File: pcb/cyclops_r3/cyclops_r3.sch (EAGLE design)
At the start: 120 parts, among them Q1 BC817-16SMD, Q2 IRF540, U1 MCP4921, U10 AD829, U11 MIC5225, U12 MIC5270, U2 317-N, U3 TLV3701, U4 337-N, U5 ADR03, U6 OP1177, U7 TLV2374, U8 ZXTD45, U9 ADA4899

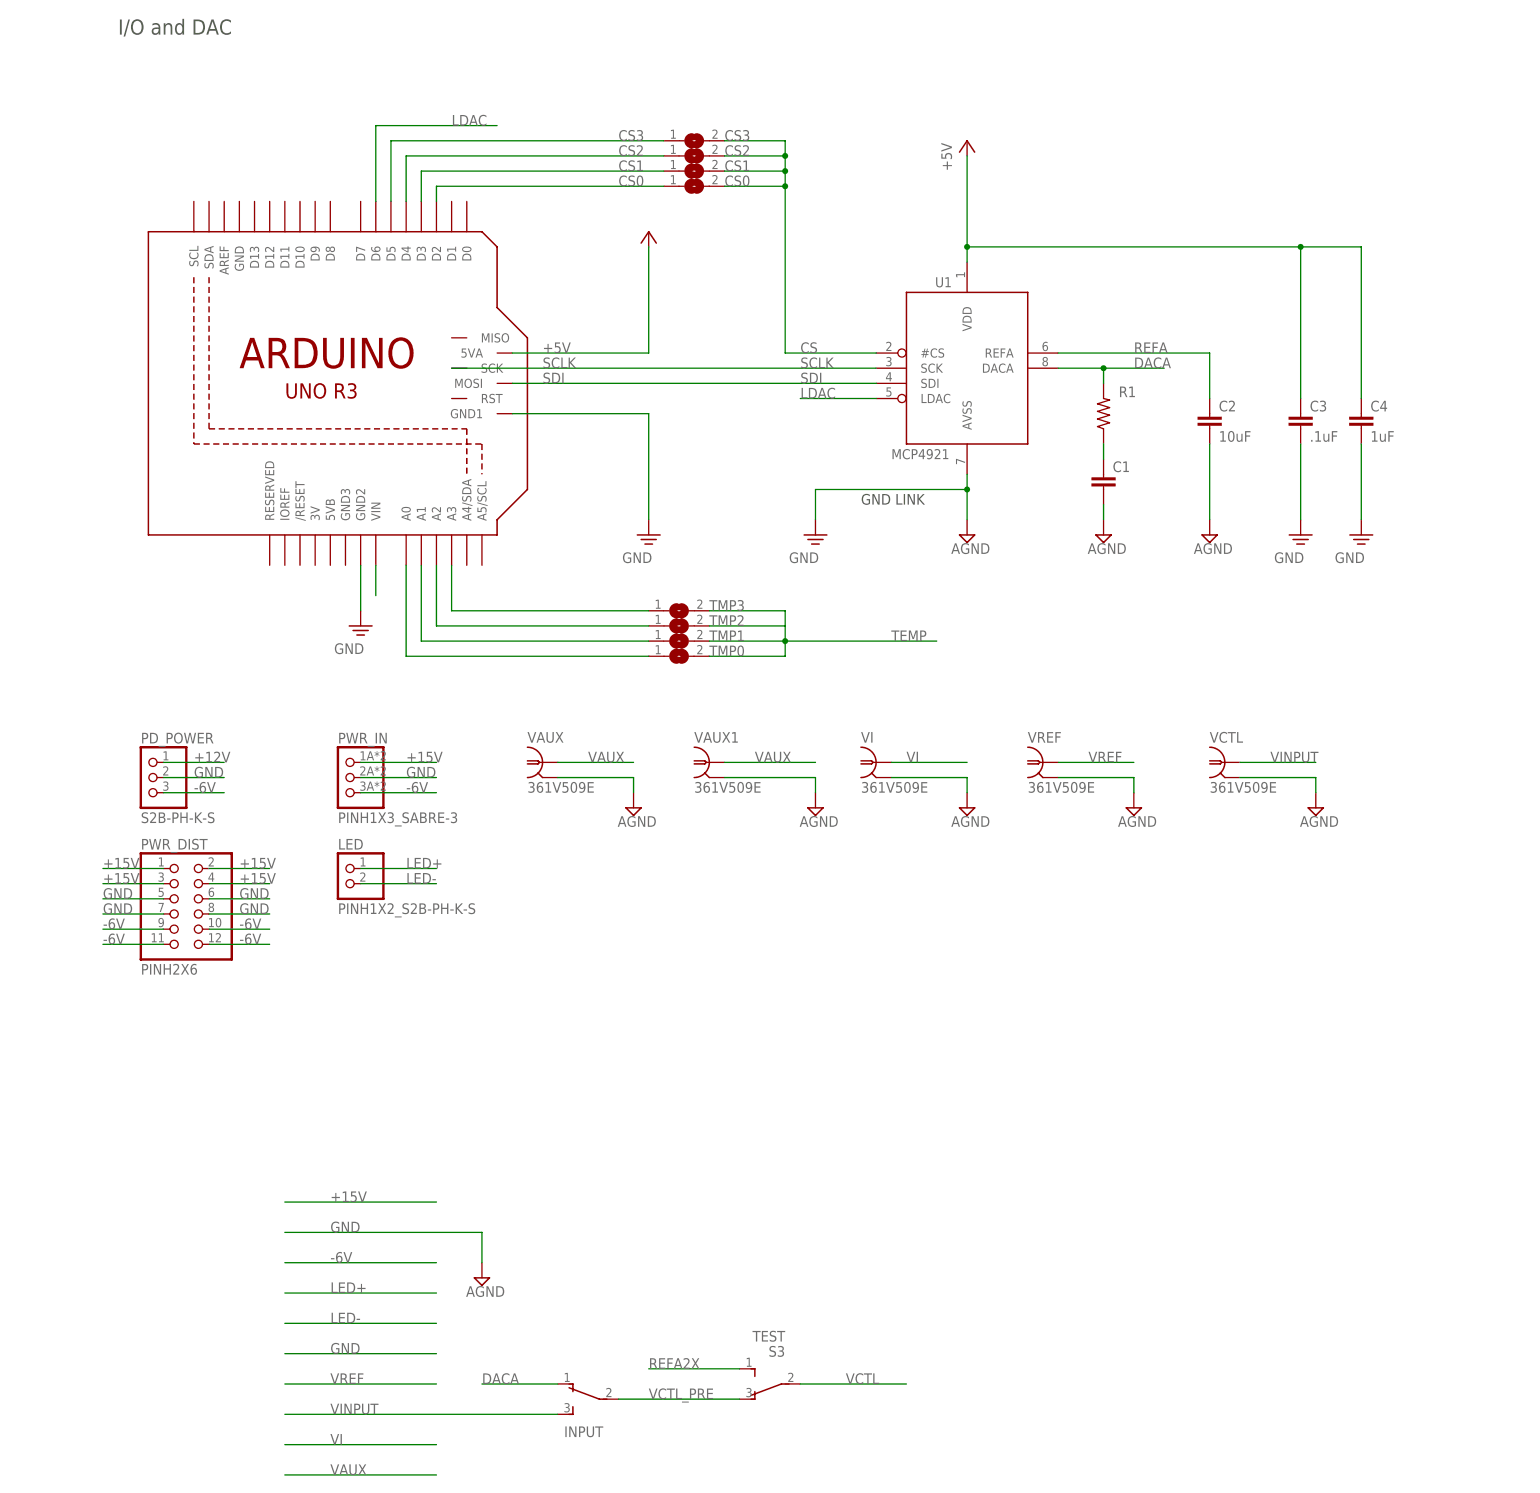
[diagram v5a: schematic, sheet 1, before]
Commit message: Finished basic layout. Need to go through notes and check things off. Need to perform ERC and DRC. Need to finish silkscreen.
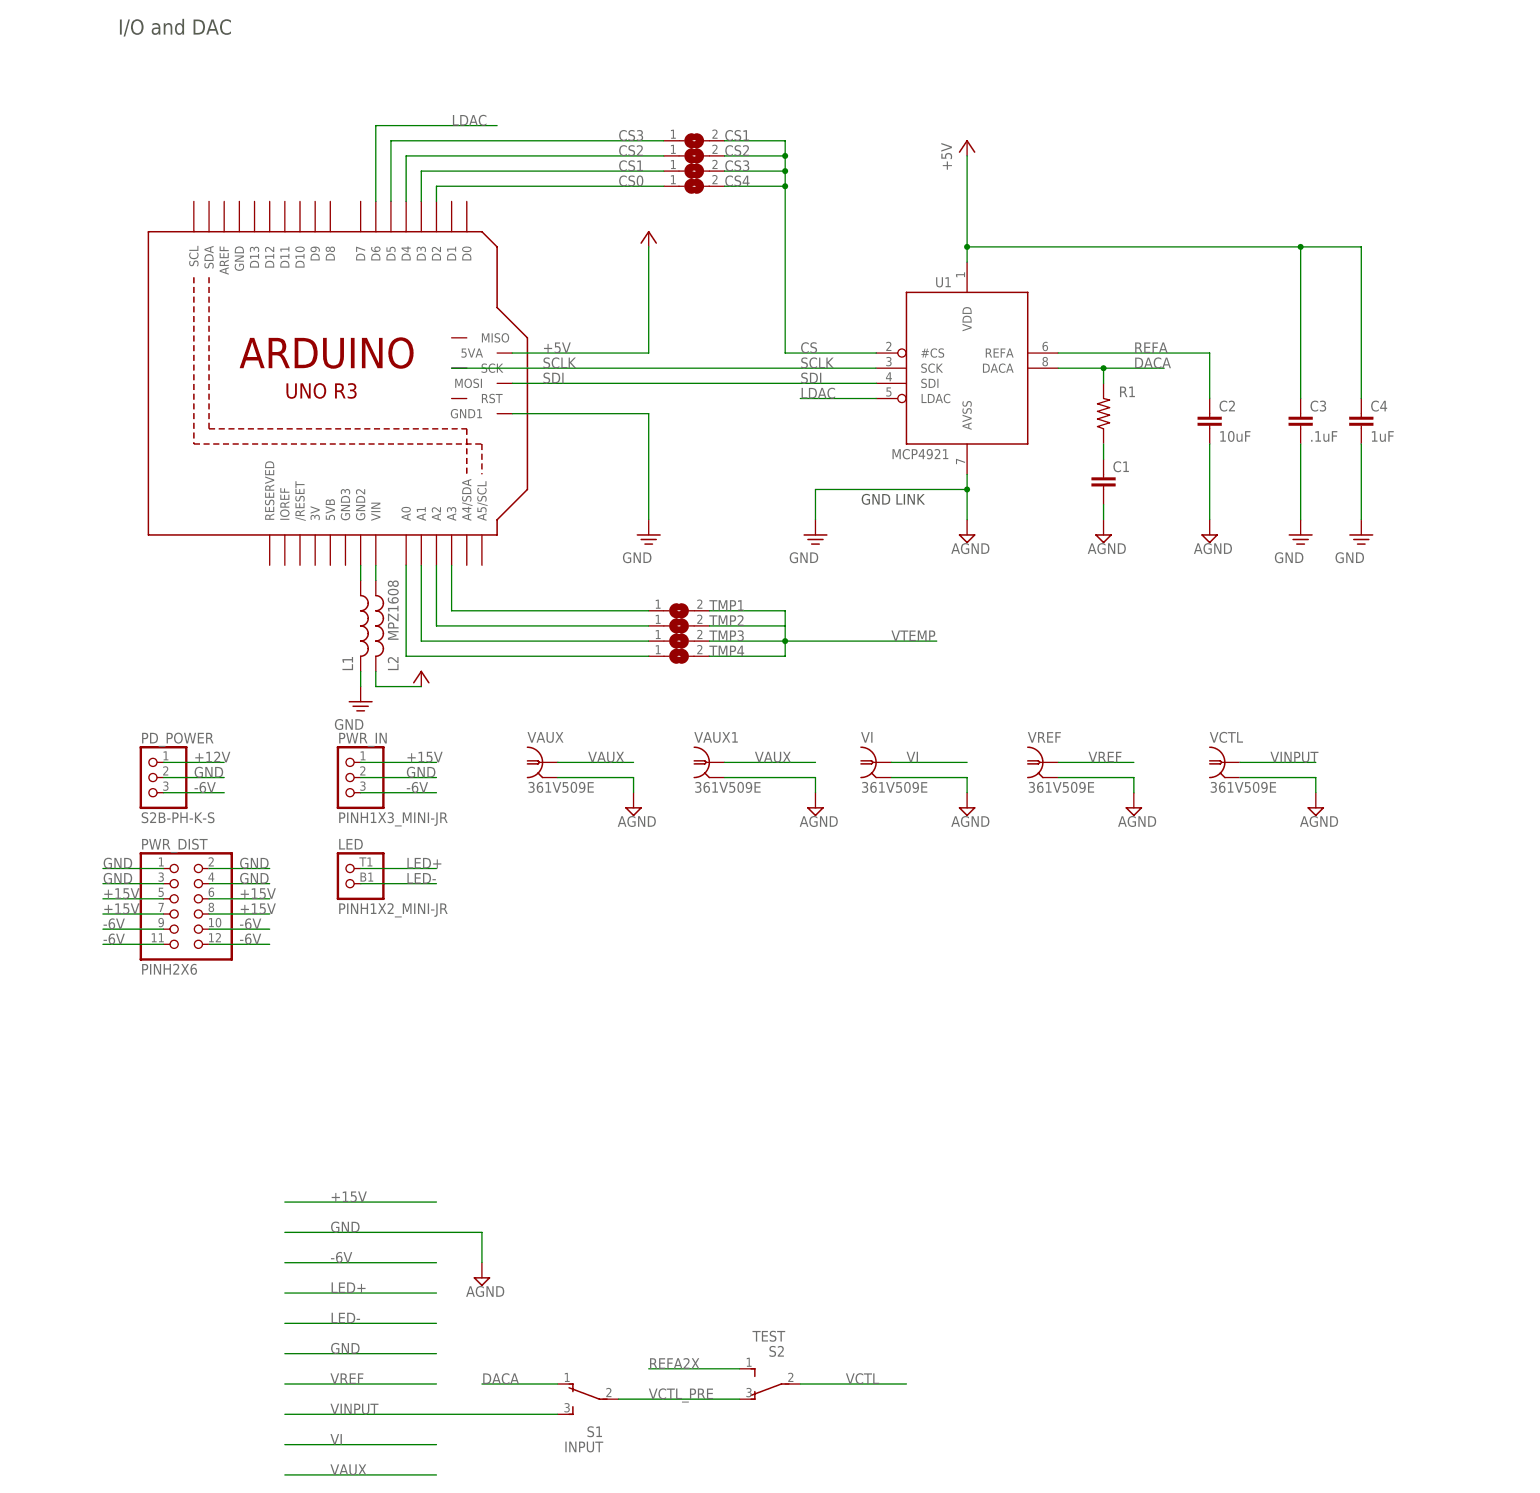
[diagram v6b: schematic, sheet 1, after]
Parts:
- removed D5: VBPW34S, cyclops:PHOTODIODE_VBPW34S
- removed R28: 140, cyclops:R_0603
- removed R29: 237, cyclops:R_0603
- removed R30: 79, cyclops:R_0603
- removed S5: CURR/AUX, cyclops:SPDT_JS
- added D1: S1B, cyclops:DIODES1B-13-F
- added L1, L2: MPZ1608, cyclops:L_0805
- added R10: 75, cyclops:R_0603
- added R6: 2.1k, cyclops:R_0603
- added R7: 10k, cyclops:R_0603
- added S2: TEST, cyclops:SPDT_CFPA
- C19: value .1uF -> (none)
- C20, C29, C34: value 1uF -> .1uF; device cyclops:C_0805 -> cyclops:C_0603
- C21: value (none) -> .1uF
- C23, C25: value 10uF -> 1uF; device cyclops:C-POL_6032M -> cyclops:C_0805
- C24: value 1uF -> 10uF; device cyclops:C_0805 -> cyclops:C-POL_6032M
- C26: value 15pF -> 10uF; device cyclops:C_0603 -> cyclops:C-POL_6032M
- C27: value .1uF -> 15pF
- C30: value 56pF -> 1uF; device cyclops:C_0603 -> cyclops:C_0805
- C31: value 1uF -> 56pF; device cyclops:C_0805 -> cyclops:C_0603
- C32: value .1uF -> 10pF
- C33, C36: value .1uF -> 1uF; device cyclops:C_0603 -> cyclops:C_0805
- C35: value 10pF -> .1uF
- D2: value S1B -> DS11015; device cyclops:DIODES1B-13-F -> cyclops:S-DIODESOD-123
- D4: value DS11015 -> VBPW34S; device cyclops:S-DIODESOD-123 -> cyclops:PHOTODIODE_VBPW34S
- LED: value PINH1X2_S2B-PH-K-S -> PINH1X2_MINI-JR; device cyclops:PINH1X2_S2B-PH-K-S -> cyclops:PINH1X2_MINI-JR
- PWR_IN: value PINH1X3_SABRE-3 -> PINH1X3_MINI-JR; device cyclops:PINH1X3_SABRE-3 -> cyclops:PINH1X3_MINI-JR
- R11: value 1k -> 120
- R12: value 3k -> 470
- R13: value 75 -> 1k
- R14: value 120 -> 1k
- R15: value 470 -> 1k
- R18: value 1k -> 9k 0.1%
- R19: value 1k -> 1k 0.1%
- R20: value 1k -> 10
- R21: value 1k 0.1% -> 1k
- R22: value 9k 0.1% -> 1.24k
- R23: value 10 -> 20k
- R24: value 1k -> 4.3k
- R25: value 1.24k -> 140
- R26: value 20k -> 237
- R27: value 4.3k -> 79
- R3: value 10k -> 110k
- R4: value 110k -> 10k
- R5: value 10k -> 240
- R8: value 240 -> 1k
- R9: value 2.1k -> 3k
- S1: value (none) -> INPUT
- S3: value TEST -> CURR/AUX; device cyclops:SPDT_CFPA -> cyclops:SPDT_JS
- U10: value AD829 -> MIC5225; device cyclops:AD829JRZ -> cyclops:MIC5225
- U11: value MIC5225 -> AD829; device cyclops:MIC5225 -> cyclops:AD829JRZ
- renumbered CS0 to CS4, INPUT to S1, REF-2.5 to REF-2.1, TMP0 to TMP4
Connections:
- new net N$11: ARDUNIO.GND2, L1.1
- new net N$14: ARDUNIO.VIN, L2.1
- net +12V: now also C22.1, C25.1, D1.A, D2.C, L2.2, R3.1, R5.2, R9.2, U10.+IN, U10.EN; no longer ARDUNIO.VIN, C19.1, C24.1, D2.A, D3.C, R11.2, R12.2, R4.1, U11.+IN, U11.EN
- net +15V: now also D1.C, PWR_DIST.5, PWR_DIST.6, PWR_DIST.7, PWR_DIST.8; no longer D2.C, PWR_DIST.1, PWR_DIST.2, PWR_DIST.3, PWR_DIST.4
- net +7V: now also C24.+, C30.1, C34.1, R23.1, U10.+OUT, U11.+VS; no longer C23.+, C29.1, C32.1, R26.1, U10.+VS, U11.+OUT
- net -2.1V: now also C21.1, C23.1, R11.1; no longer C22.1, C36.1, R14.1
- net -5V: now also C26.-, C29.1, C35.1, C36.1, D4.A, U11.-VS; no longer C25.-, C27.1, C33.1, C34.1, D5.A, U10.-VS
- net -6V: now also C33.1; no longer C31.1
- net CS1: now also CS3.1; no longer CS1.1
- net CS3: now also CS1.1; no longer CS3.1
- net CS5: now also TMP3.1; no longer TMP1.1
- net CS6: now also TMP1.1; no longer TMP3.1
- net GND: now also C21.2, C23.2, C24.-, C25.2, C26.+, D3.A, L1.2, PWR_DIST.1, PWR_DIST.2, PWR_DIST.3, PWR_DIST.4, R10.2, R13.1, R14.2, R19.2, R21.1, R24.2, R27.1, R4.2, R6.1, U10.GND; no longer ARDUNIO.GND2, C19.2, C23.-, C24.2, C25.+, C27.2, D4.A, PWR_DIST.5, PWR_DIST.6, PWR_DIST.7, PWR_DIST.8, R13.2, R16.1, R18.2, R21.2, R24.1, R27.2, R30.1, R5.2, R9.1, U11.GND
- net LED-: now also U7C.+IN; no longer U7B.+IN
- net N$10: now also R20.1; no longer R23.1
- net N$12: now also R10.1, R11.2; no longer R13.1, R14.2
- net N$13: now also R20.2, R21.2; no longer R23.2, R24.2
- net N$15: now also C19.2, R18.1, R19.1, U7C.-IN; no longer C21.2, R21.1, R22.1, U7B.-IN
- net N$16: now also C27.1, R22.2; no longer C26.1, R25.2
- net N$17: now also C27.2, R22.1; no longer C26.2, R25.1
- net N$18: now also U11.OFS_2; no longer U10.OFS_2
- net N$19: now also D4.C; no longer D5.C
- net N$2: now also R8.1; no longer R11.1
- net N$20: now also R12.2; no longer R15.2
- net N$21: now also R25.1; no longer R28.1
- net N$22: now also R12.1; no longer R15.1
- net N$23: now also R23.2, R24.1, U10.ADJ; no longer R26.2, R27.1, U11.ADJ
- net N$24: now also R26.2, R27.2, U11.-IN; no longer R29.2, R30.2, U10.-IN
- net N$25: now also U11.OFS; no longer U10.OFS
- net N$26: now also C32.1, U11.CCOMP; no longer C35.1, U10.CCOMP
- net N$27: now also R7.2; no longer R3.2
- net N$28: now also R7.1; no longer R3.1
- net N$3: now also R9.1; no longer R12.1
- net N$4: now also U7B.OUT; no longer U7C.OUT
- net N$5: now also R3.2, R4.1; no longer R4.2, R5.1
- net N$6: now also R13.2; no longer R16.2
- net N$7: now also R16.1; no longer R19.1
- net N$72: now also R5.1, R6.2; no longer R8.1, R9.2
- net N$8: now also R14.1, R15.2; no longer R17.2, R18.1
- net REFA2X: now also R17.2, S2.3; no longer R20.2, S3.3
- net TEMP: no longer TMP1.2, TMP2.2, TMP3.2, TMP4.2
- net VAUX: now also S3.3; no longer S5.3
- net VCTL: now also S2.2; no longer S3.2
- net VCTL_PRE: now also S2.1; no longer S3.1
- net VFB: now also S3.2, U7B.-IN; no longer S5.2, U7C.-IN
- net VI: now also C19.1, R18.2, S3.1, U7C.OUT; no longer C21.1, R22.2, S5.1, U7B.OUT
- net VPD: now also R26.1, U11.OUTPUT; no longer R29.1, U10.OUTPUT
- net VPD_PRE: now also C31.1, R25.2, U11.+IN; no longer C30.1, R28.2, U10.+IN
- net VREFA2X: now also R15.1; no longer R20.1
- net VTEMP: now also TMP1.2, TMP2.2, TMP3.2, TMP4.2
- net _VREF: now also D2.A, D3.C, R16.2, U7B.+IN; no longer D3.A, D4.C, R19.2, U7C.+IN
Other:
- moved on the sheet: C19, C20, C21, C22, C24, C25, C26, C27, C29, C30, C31, C32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

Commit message: Added IDC header for LED module.
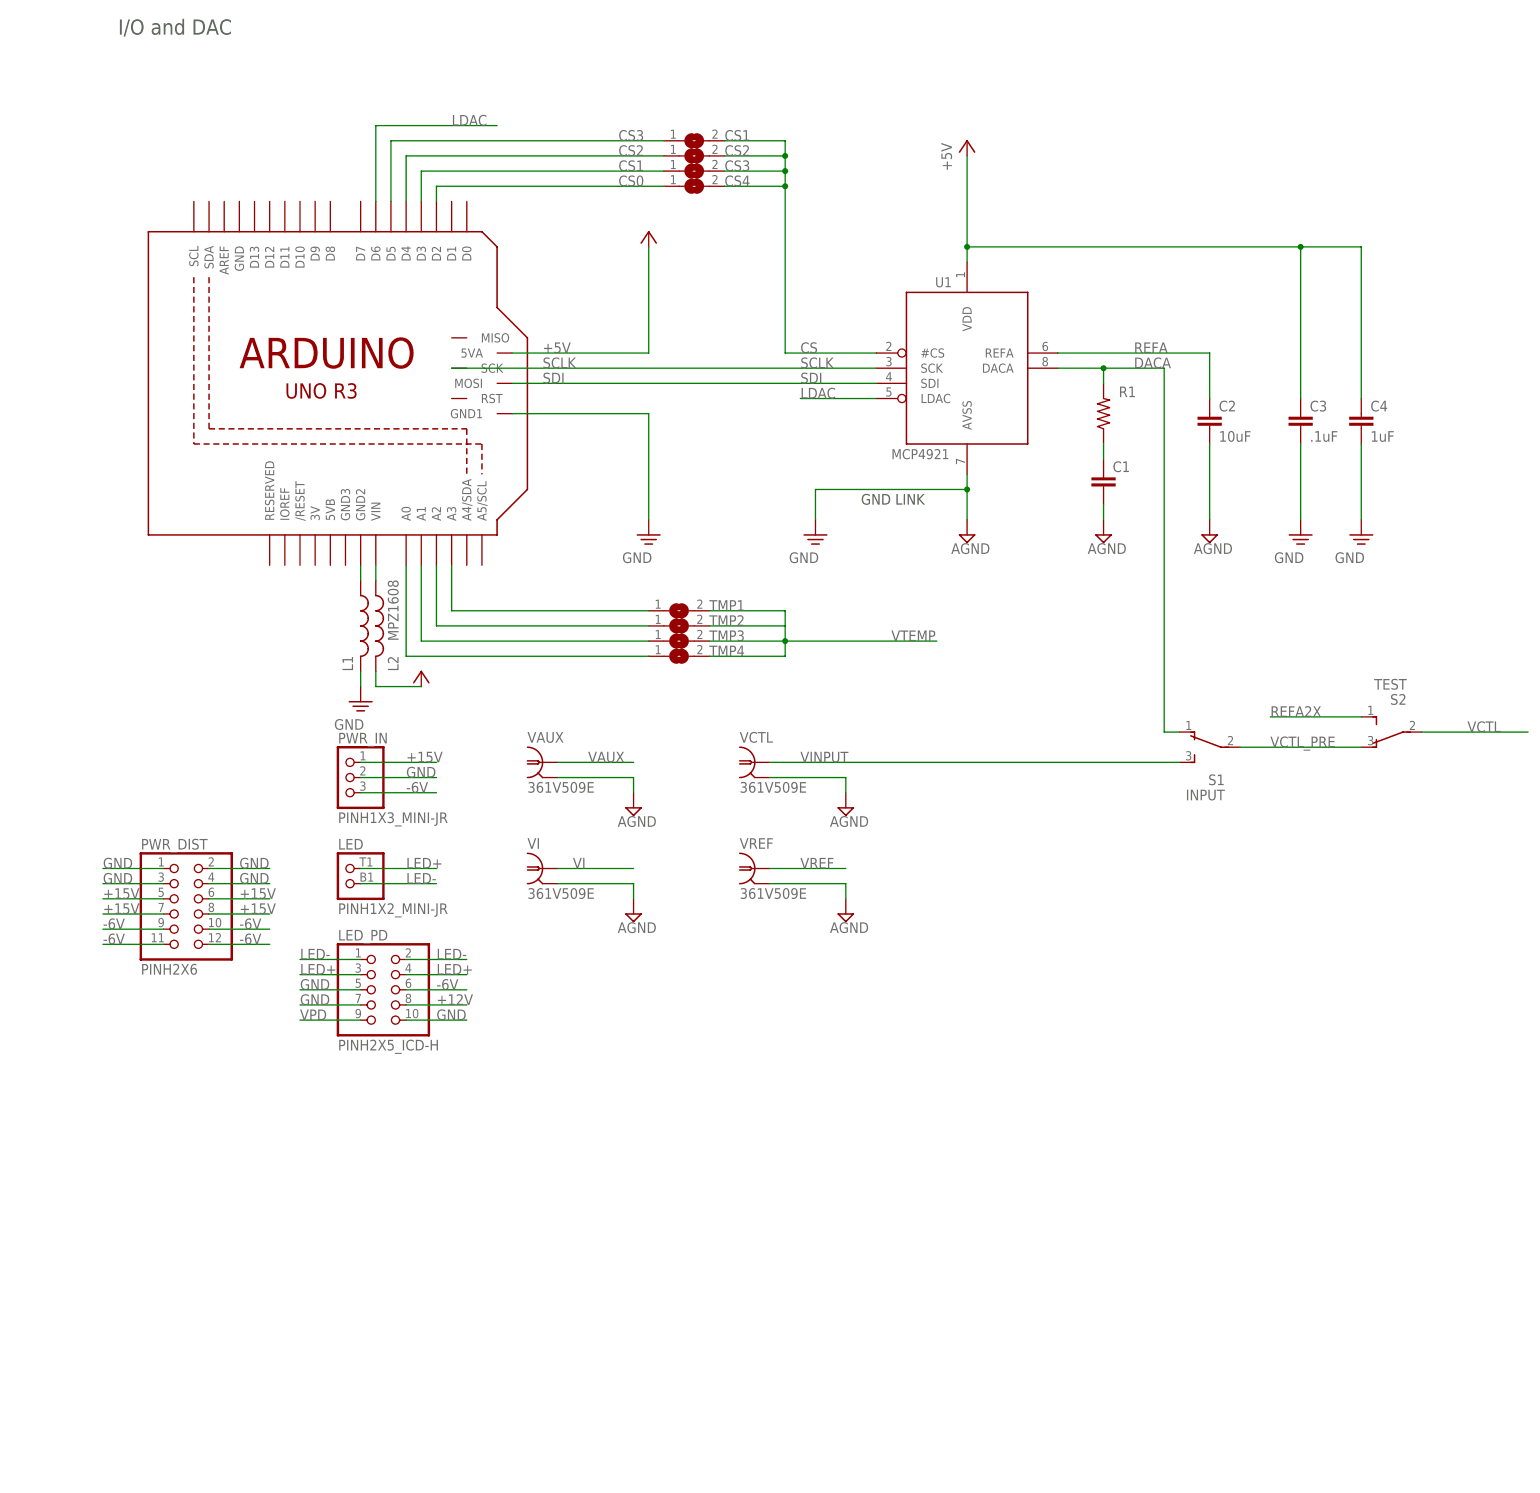
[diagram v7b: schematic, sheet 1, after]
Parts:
- removed PD_POWER: S2B-PH-K-S, cyclops:PINH1X3_S3B-PH-K-S
- removed VAUX1: 361V509E, cyclops:BNC_V-BITE
- added LED_PD: PINH2X5_ICD-H, cyclops:PINH2X5_ICD-H
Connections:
- net +12V: now also LED_PD.8; no longer PD_POWER.1
- net -6V: now also LED_PD.6; no longer PD_POWER.3
- net GND: now also LED_PD.10, LED_PD.5, LED_PD.7; no longer PD_POWER.2, VAUX1.2
- net LED+: now also LED_PD.3, LED_PD.4
- net LED-: now also LED_PD.1, LED_PD.2
- net VAUX: no longer VAUX1.1
- net VPD: now also LED_PD.9
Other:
- moved on the sheet: S1, S2, VCTL, VI, VREF
